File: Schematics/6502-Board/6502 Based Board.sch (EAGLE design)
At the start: 19 parts, among them IC1 74HC14N, IC2 74HC74N, Q1 4MHz, U1 W65C02S-DIP

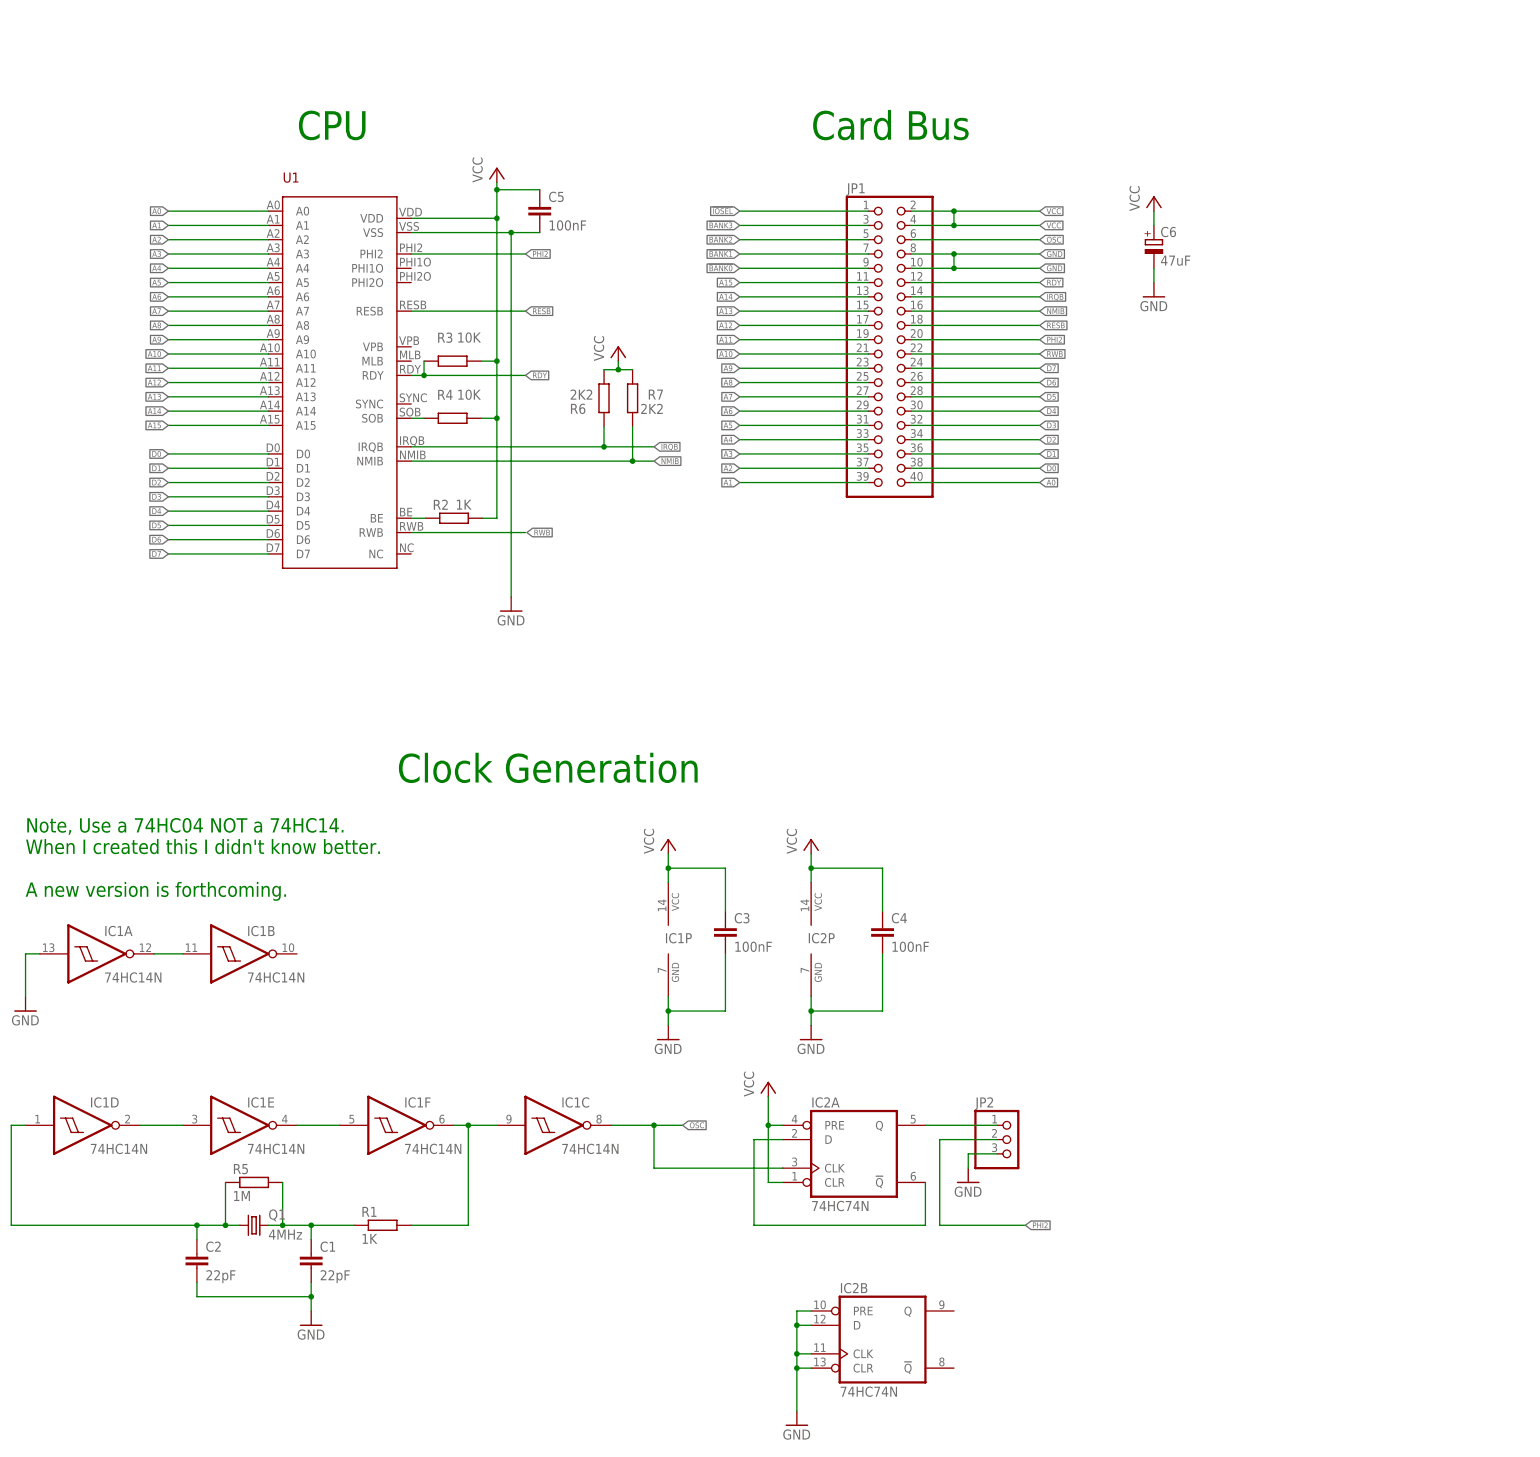
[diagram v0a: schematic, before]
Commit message: Updated the processor board to add the following features:-
Added a header for NMI and IRQ status lights.

Reworked the circuit and added a header to allow 1, 2 and 4MHz clock speeds from the on-board oscillator.
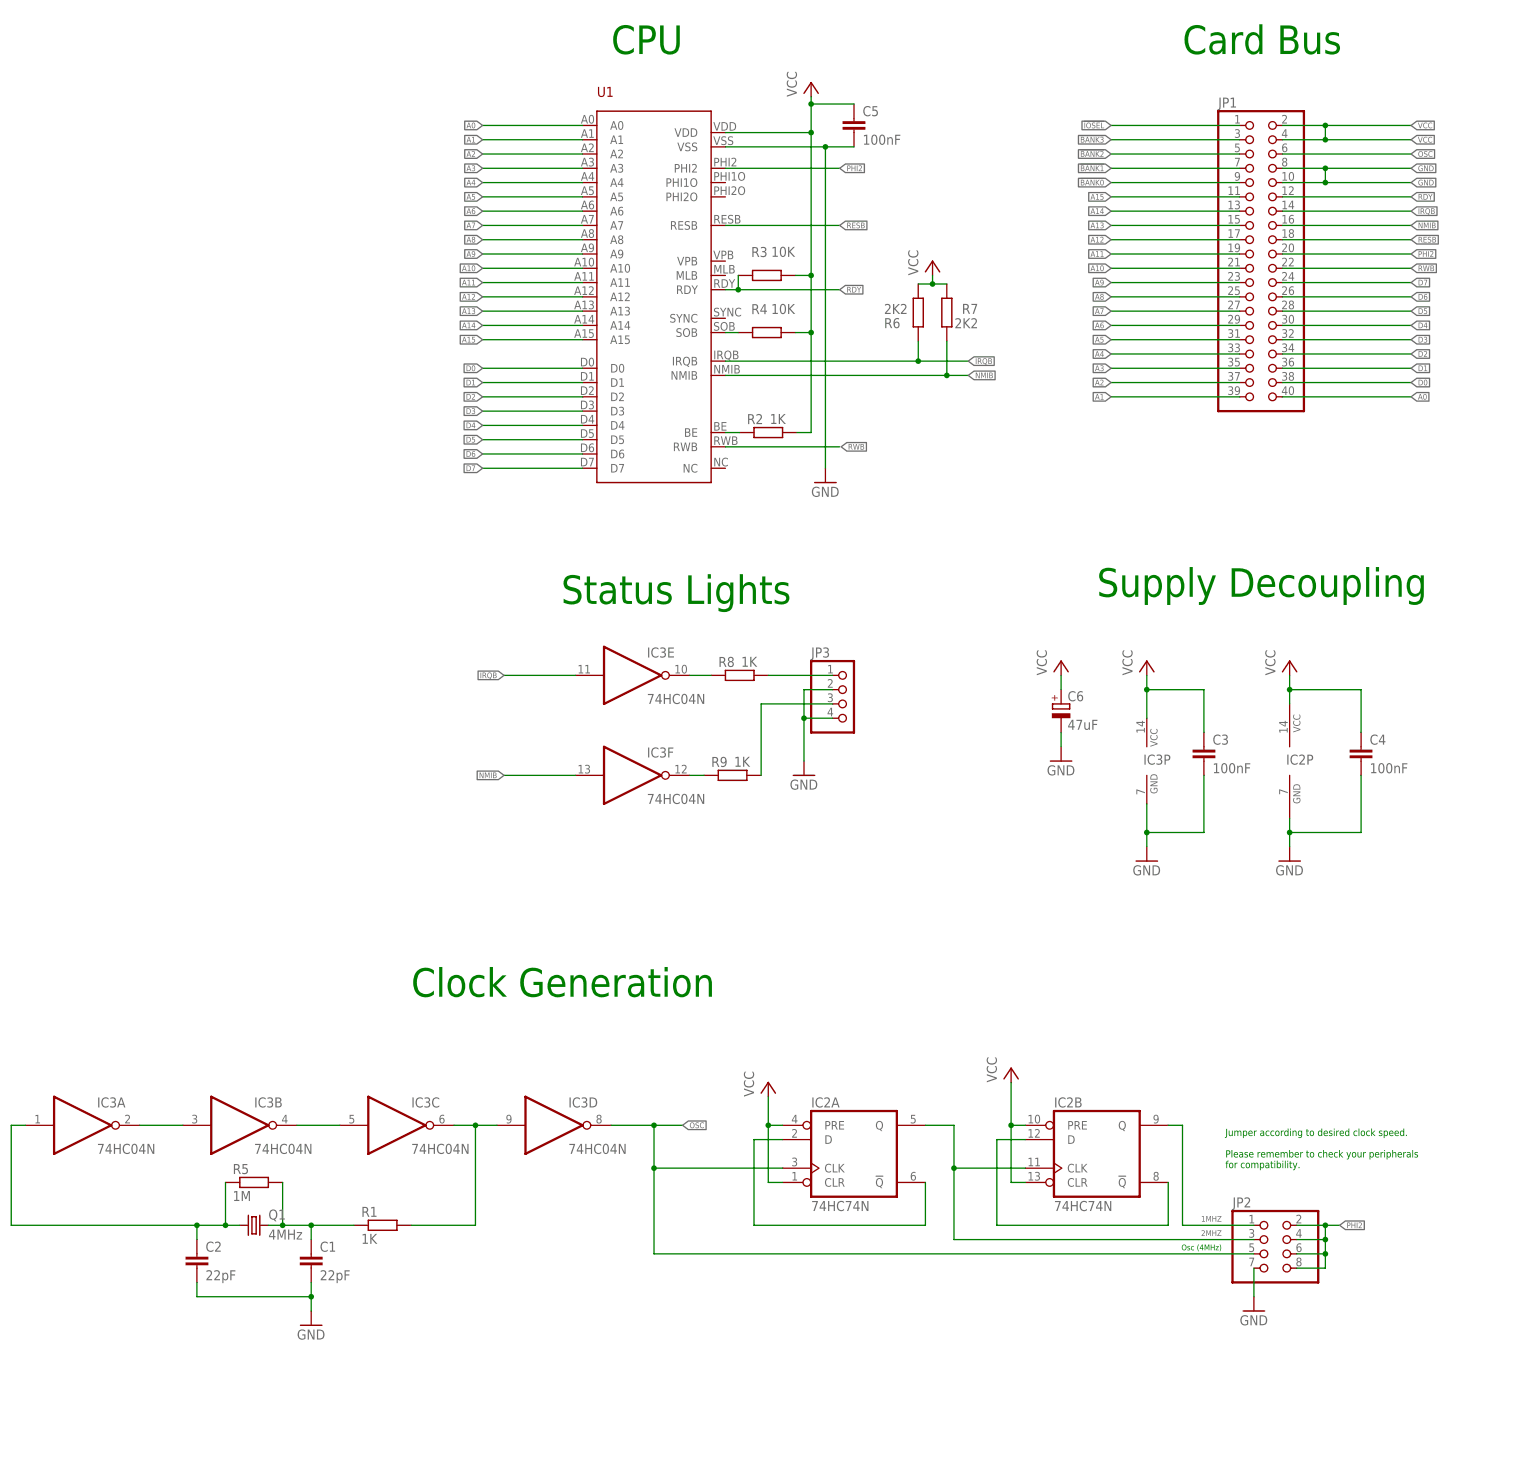
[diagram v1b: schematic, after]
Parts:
- removed IC1: 74HC14N, 74xx-us:7414N
- added IC3: 74HC04N, 74xx-eu:74HC04N
- added JP3: (no value), pinhead:PINHD-1X4/90
- added R8, R9: 1K, rcl:R-EU_0207/2V
- JP2: device pinhead:PINHD-1X3 -> pinhead:PINHD-2X4
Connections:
- removed net N$6: IC1A.O, IC1B.I
- removed net PHI2_OUT: IC2A.Q, JP2.1
- new net 1MHZ: IC2B.Q, JP2.1
- new net 2MHZ: IC2A.Q, IC2B.CLK, JP2.3
- new net IRQ_LED: JP3.1, R8.2
- new net N$11: IC3E.O, R8.1
- new net N$12: IC3F.O, R9.1
- new net N$8: IC2B.!Q, IC2B.D
- new net NMI_LED: JP3.3, R9.2
- net GND: now also IC3P.GND, JP2.7, JP3.2, JP3.4; no longer IC1A.I, IC1P.GND, IC2B.CLK, IC2B.CLR, IC2B.D, IC2B.PRE, JP2.3
- net IRQB: now also IC3E.I
- net N$2: now also IC3B.O, IC3C.I; no longer IC1E.O, IC1F.I
- net N$3: now also IC3C.O, IC3D.I; no longer IC1C.I, IC1F.O
- net N$5: now also IC3A.I; no longer IC1D.I
- net N$7: now also IC3A.O, IC3B.I; no longer IC1D.O, IC1E.I
- net NMIB: now also IC3F.I
- net OSC: now also IC3D.O, JP2.5; no longer IC1C.O
- net PHI2: now also JP2.4, JP2.6, JP2.8
- net VCC: now also IC2B.CLR, IC2B.PRE, IC3P.VCC; no longer IC1P.VCC
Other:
- note added: "Jumper according to desired clock speed. Please remember to check your peripherals for compatibility."
- note added: "Osc (4MHz)"
- note added: "Status Lights"
- note added: "Supply Decoupling"
- note removed: "Note, Use a 74HC04 NOT a 74HC14. When I created this I didn't know better. A new version is forthcoming."
- moved on the sheet: C3, C4, C5, C6, IC2B, IC2P, JP1, R2, R3, R4, R6, R7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
